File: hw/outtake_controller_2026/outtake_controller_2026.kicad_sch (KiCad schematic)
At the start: 5 parts, among them J1 1935174, J2 1935187, J3 1935161, J4 1935174

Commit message: ManteakaMohoOuttakeEdits
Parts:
- U1: footprint (none) -> outtake_controller_2026_footprints:LogicFET_DMN24H3D5L
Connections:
- net LMD18200/M_BOOT1: now also J4.1
- net LMD18200/M_BOOT2: now also J4.2
- net LMD18200/M_CFLAG: now also J2.2
- net LMD18200/M_DIR: now also J1.1
- net LMD18200/M_PWM: now also J1.2
- net LMD18200/M_TFLAG: now also J2.1
- net at U1.1 (SRC): now also J1.3
- net at U1.3 (DRAIN): now also J3.1
- net GND: now reaches J4.3
- net GND: now also J3.2

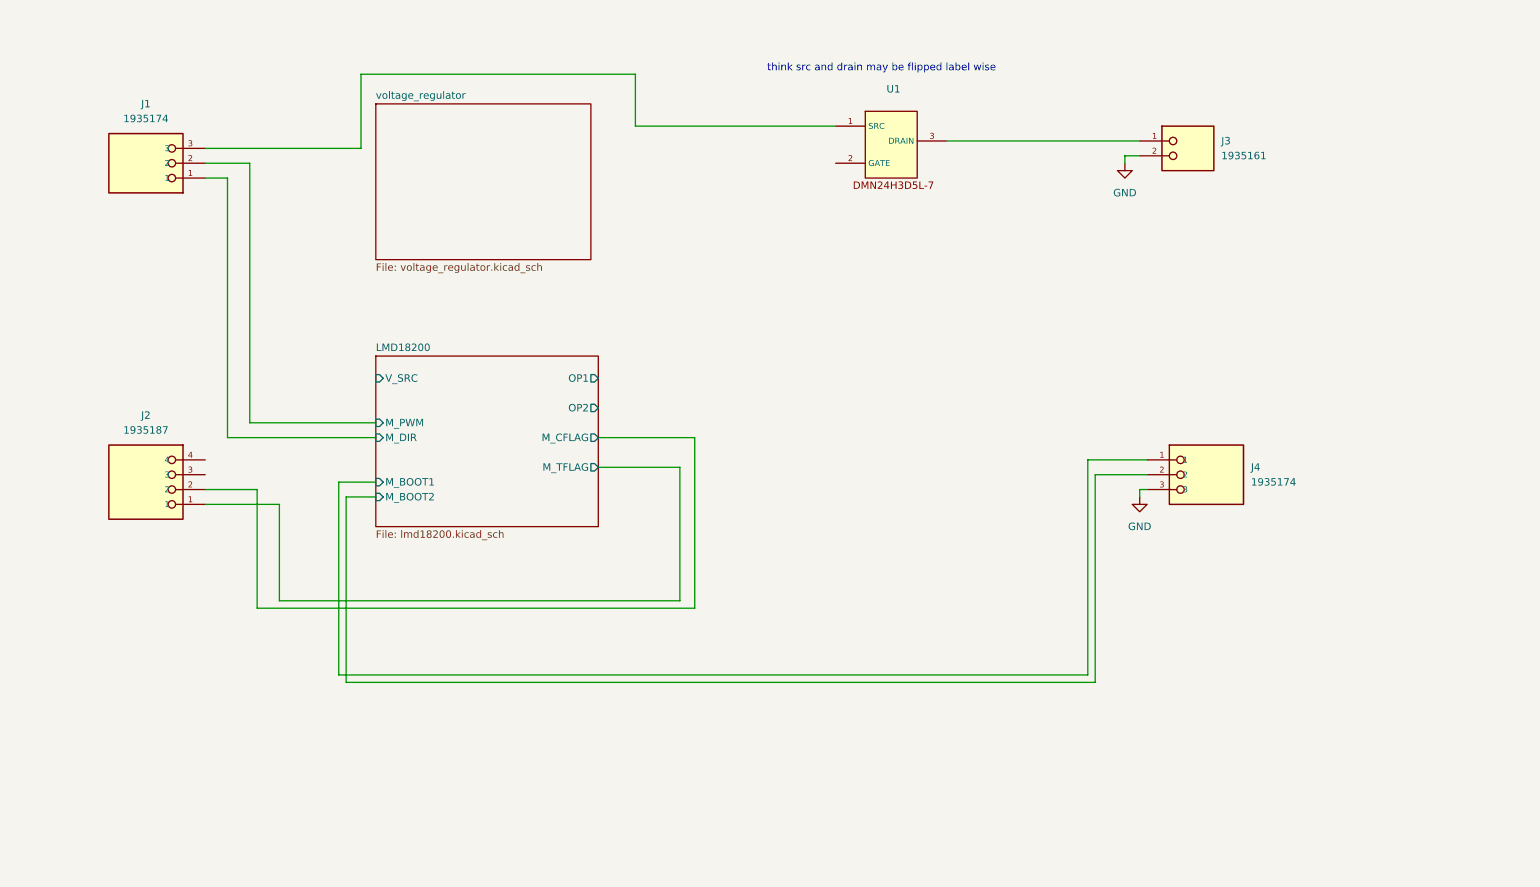
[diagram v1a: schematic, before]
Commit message: finished actuator board, includes zip folder of project and gerbers used to order board
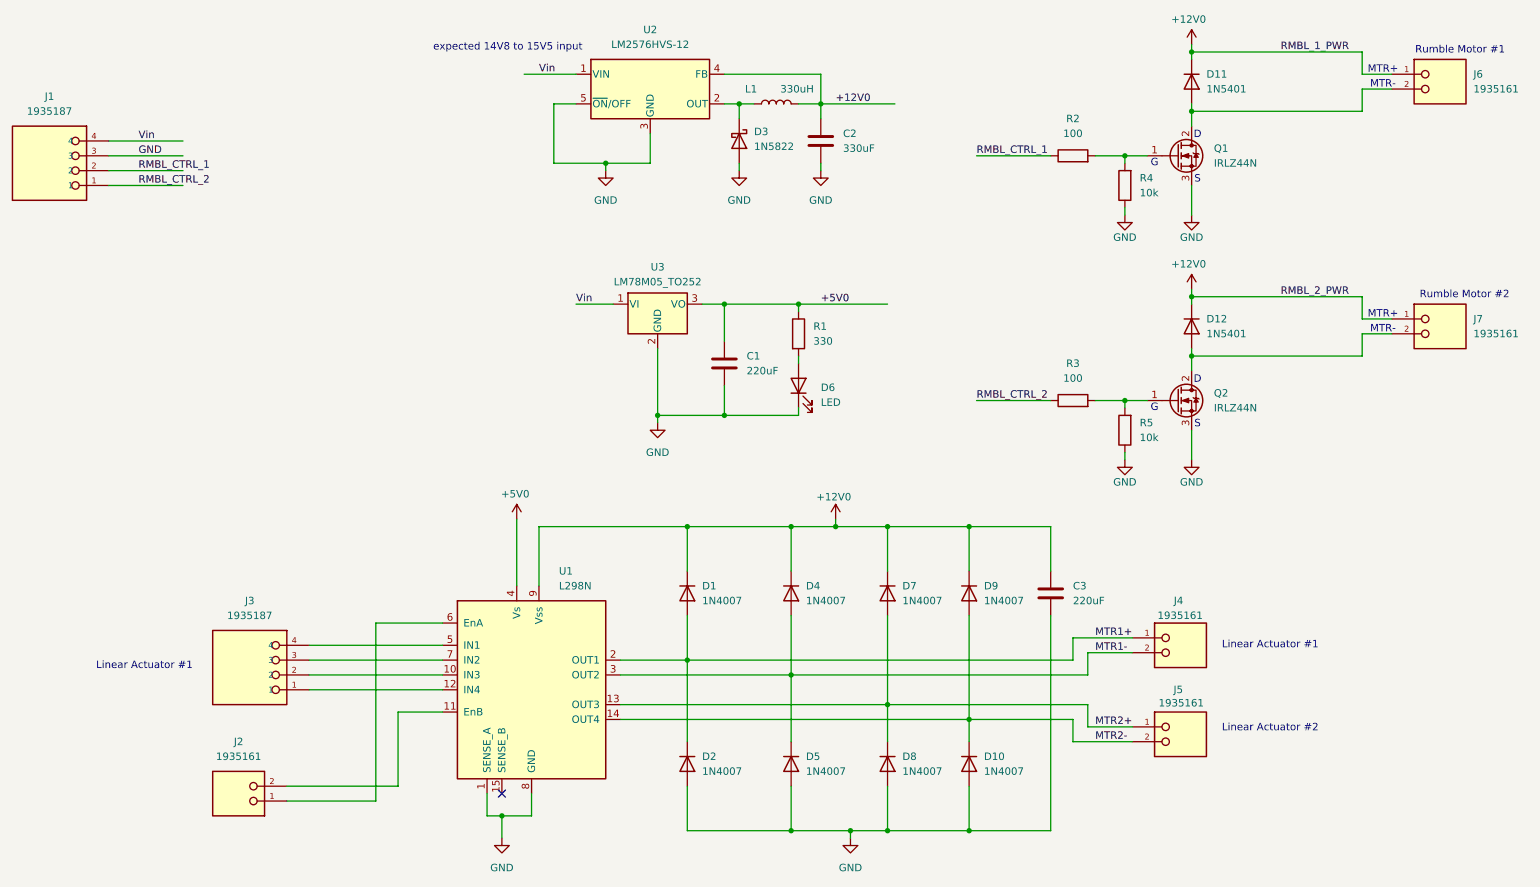
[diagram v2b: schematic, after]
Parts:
- removed J1, J4: 1935174, 1935174:PHOENIX_1935174, symbol outtake_controller_2026_parts_library:1935174
- removed J2: 1935187, 1935187:PHOENIX_1935187, symbol outtake_controller_2026_parts_library:1935187
- removed J3: 1935161, 1935161:PHOENIX_1935161, symbol outtake_controller_2026_parts_library:1935161
- removed U1: ~, outtake_controller_2026_footprints:LogicFET_DMN24H3D5L, symbol outtake_controller_2026_parts_library:DMN24H3D5L-7
- added C1, C3: 220uF, Capacitor_THT:C_Radial_D5.0mm_H11.0mm_P2.00mm, symbol Device:C
- added C2: 330uF, Capacitor_THT:C_Radial_D5.0mm_H11.0mm_P2.00mm, symbol Device:C
- added D1, D10, D2, D4, D5, D7, D8, D9: 1N4007, Diode_THT:D_DO-41_SOD81_P10.16mm_Horizontal, symbol Diode:1N4007
- added D11, D12: 1N5401, Diode_THT:D_DO-201AD_P15.24mm_Horizontal, symbol Diode:1N5401
- added D3: 1N5822, Diode_THT:D_DO-201AD_P15.24mm_Horizontal, symbol Diode:1N5822
- added D6: LED, LED_THT:LED_D5.0mm, symbol Device:LED
- added J1, J3: 1935187, outtake_controller_2026_footprints:ScrewTerminal_4Block_1935187_PhoenixContact, symbol outtake_controller_2026_parts_library:1935187
- added J2, J4, J5, J6, J7: 1935161, outtake_controller_2026_footprints:ScrewTerminal_2Block_1935161_PhoenixContact, symbol outtake_controller_2026_parts_library:1935161
- added L1: 330uH, Inductor_THT:L_Axial_L9.5mm_D4.0mm_P12.70mm_Horizontal_Fastron_SMCC, symbol Device:L
- added Q1, Q2: IRLZ44N, Package_TO_SOT_THT:TO-220-3_Vertical, symbol Transistor_FET:IRLZ44N
- added R1: 330, Resistor_THT:R_Axial_DIN0207_L6.3mm_D2.5mm_P10.16mm_Horizontal, symbol Device:R
- added R2, R3: 100, Resistor_THT:R_Axial_DIN0207_L6.3mm_D2.5mm_P10.16mm_Horizontal, symbol Device:R
- added R4, R5: 10k, Resistor_THT:R_Axial_DIN0207_L6.3mm_D2.5mm_P10.16mm_Horizontal, symbol Device:R
- added U1: L298N, Package_TO_SOT_THT:TO-220-15_P2.54x5.08mm_StaggerOdd_Lead4.58mm_Vertical, symbol Driver_Motor:L298N
- added U2: LM2576HVS-12, Package_TO_SOT_SMD:TO-263-5_TabPin3, symbol Regulator_Switching:LM2576HVS-12
- added U3: LM78M05_TO252, Package_TO_SOT_SMD:TO-252-2, symbol Regulator_Linear:LM78M05_TO252
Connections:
- net GND: now also C1.2, C2.2, C3.2, D10.2 (A), D2.2 (A), D3.2 (A), D5.2 (A), D6.1 (K), D8.2 (A), J1.3, Q1.3 (S), Q2.3 (S), R4.1, R5.1, U1.1 (SENSE_A), U1.8 (GND), U2.3 (GND), U2.5 (~{ON}/OFF), U3.2 (GND)
- new net: D12.2 (A), J7.2, Q2.2 (D)
- new net: D6.2 (A), R1.2
- new net: D3.1 (K), L1.1, U2.2 (OUT)
- new net: Q2.1 (G), R3.2, R5.2
- new net: Q1.1 (G), R2.2, R4.2
- new net: J3.2, U1.10 (IN3)
- new net: J2.2, U1.11 (EnB)
- new net: J3.1, U1.12 (IN4)
- new net: J3.4, U1.5 (IN1)
- new net: J2.1, U1.6 (EnA)
- new net: J3.3, U1.7 (IN2)
- new net: D11.2 (A), J6.2, Q1.2 (D)
- new net +12V0: C2.1, C3.1, D1.1 (K), D11.1 (K), D12.1 (K), D4.1 (K), D7.1 (K), D9.1 (K), J6.1, J7.1, L1.2, U1.9 (Vss), U2.4 (FB)
- new net +5V0: C1.1, R1.1, U1.4 (Vs), U3.3 (VO)
- new net MTR1+: D1.2 (A), D2.1 (K), J4.1, U1.2 (OUT1)
- new net MTR1-: D4.2 (A), D5.1 (K), J4.2, U1.3 (OUT2)
- new net MTR2+: D7.2 (A), D8.1 (K), J5.1, U1.13 (OUT3)
- new net MTR2-: D10.1 (K), D9.2 (A), J5.2, U1.14 (OUT4)
- new net RMBL_CTRL_1: J1.2, R2.1
- new net RMBL_CTRL_2: J1.1, R3.1
- new net Vin: J1.4, U2.1 (VIN), U3.1 (VI)
- no-connect marks 0 -> 1
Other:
- removed sheet LMD18200
- removed sheet voltage_regulator
- note added: "D"
- note added: "G"
- note added: "Linear Actuator #1"
- note added: "Linear Actuator #2"
- note added: "MTR+"
- note added: "MTR-"
- note added: "Rumble Motor #1"
- note added: "Rumble Motor #2"
- note added: "S"
- note added: "expected 14V8 to 15V5 input"
- note removed: "think src and drain may be flipped label wise"
